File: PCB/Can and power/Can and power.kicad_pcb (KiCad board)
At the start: 2 copper layers, 37.5 x 35 mm, 34 parts, among them J1 TPS54232DR, J2 ESP32, J3 12V, J4 C_H, J5 C_L, J6 GND, U1 SN65HVD230

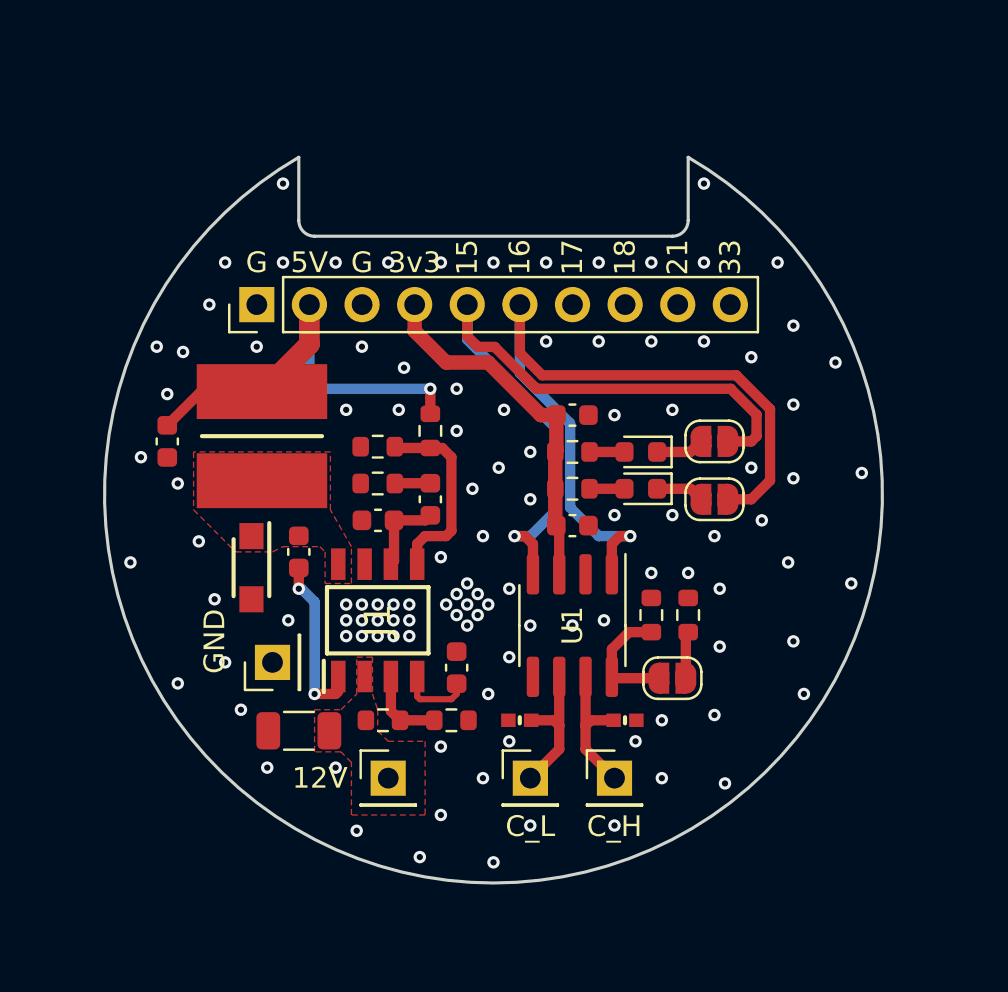
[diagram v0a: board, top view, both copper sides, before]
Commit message: Added protection diode on voltage input
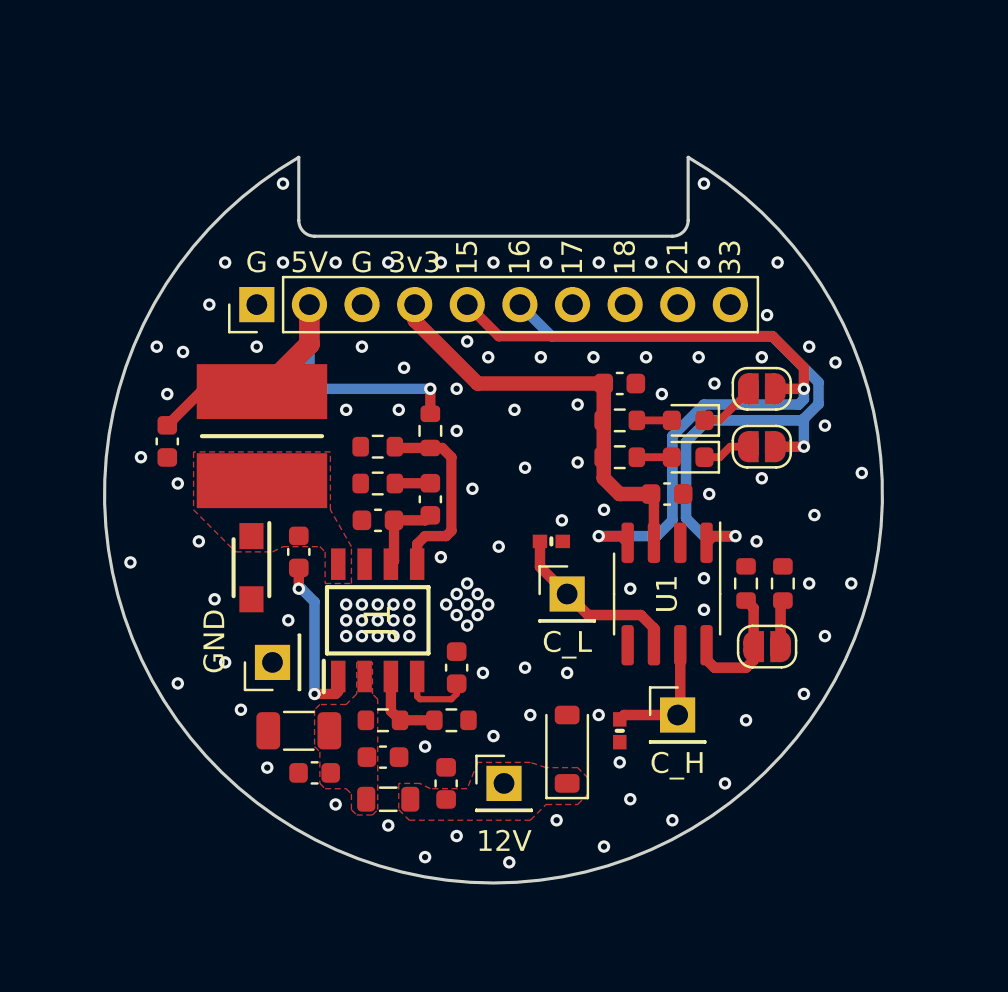
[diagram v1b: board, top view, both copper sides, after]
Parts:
- removed G***: LOGO, LOGO
- added C1: 0.1uF 50V, Capacitor_SMD:C_0603_1608Metric, F.Cu at (137.7, 114.0)
- added C2: 0.1uF 50V, Capacitor_SMD:C_0603_1608Metric, F.Cu at (134.7, 112.7)
- added C5: 1uF, Capacitor_SMD:C_0603_1608Metric, F.Cu at (131.4, 113.5)
- added D6: 18V, Diode_SMD:D_SOD-123, F.Cu at (143.6, 112.3)
- added FB1: 120R@100MHz, Inductor_SMD:L_0805_2012Metric, F.Cu at (134.9, 114.7)
- moved J5 9.07 mm to (143.6, 104.8)
- moved D2 8.77 mm to (142.8, 102.3), turned to 0 degrees
- moved J3 5.59 mm to (140.5, 114.0)
- moved C3 4.82 mm to (148.4, 100.0)
- moved JP1 4.82 mm to (153.2, 107.4)
- moved R2 4.82 mm to (154.0, 104.3)
- moved R8 4.82 mm to (152.2, 104.3)
- moved U1 4.82 mm to (148.4, 104.8)
- moved J4 4.31 mm to (148.9, 110.7)
- moved JP3 3.42 mm to (153.0, 97.7)
- moved JP2 3.42 mm to (153.0, 94.9)
- moved C4 2.75 mm to (146.1, 94.7)
- moved D4 2.75 mm to (149.4, 96.4)
- moved D5 2.75 mm to (149.4, 98.2)
- moved R1 2.75 mm to (146.1, 96.4)
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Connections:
- C9 pad 1: +12V -> Net-(J1-VIN)
- J1 pad 2: +12V -> Net-(J1-VIN)
- Ren1 pad 2: +12V -> Net-(J1-VIN)
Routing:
- net GPIO16: track 38.2 -> 34.8 mm, vias 1 -> 2
- net +3V3: track 17.6 -> 20.7 mm
- net Net-(J5-Pin_1): track 6.93 -> 8.78 mm
- net Net-(J4-Pin_1): track 6.93 -> 6.30 mm
- net GPIO15: track 36.3 -> 37.0 mm, vias 1 -> 2
- net Net-(D4-K): track 2.33 -> 2.83 mm
- added copper zone on F.Cu, net Net-(J1-VIN)

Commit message: V4 PCB
Ren1 and Ren2 values might not be discriminating enough
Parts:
- added G***: LOGO, Library:QRCode, B.Cu at (134.4, 99.5)

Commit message: Schematics and PCB update
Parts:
- D1, D2: footprint SamacSys_Parts:DIONC1005X43N -> DIY:DIONC1005X43N
- D3: footprint SamacSys_Parts:SODFL3617X108N -> DIY:SODFL3617X108N
- J1: footprint SamacSys_Parts:SOIC127P600X175-8N -> DIY:SOIC127P600X175-8N
- L2: footprint SamacSys_Parts:INDC6060X450N -> DIY:INDC6060X450N

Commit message: Universal cutout integration
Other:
- board size 37.5 x 35 mm -> 43.4 x 43.5 mm

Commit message: Pre-PCB layout
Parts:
- removed G***: LOGO, Library:QRCode
- removed J2: ESP32, Connector_PinHeader_2.54mm:PinHeader_1x10_P2.54mm_Vertical
- removed JP2, JP3: SolderJumper_2_Open, Jumper:SolderJumper-2_P1.3mm_Open_RoundedPad1.0x1.5mm
- added J7: Car connector, Connector_PinHeader_2.54mm:PinHeader_1x05_P2.54mm_Vertical, F.Cu at (137.3, 91.1)
- added JP4: Use IGN, Jumper:SolderJumper-2_P1.3mm_Bridged_RoundedPad1.0x1.5mm, B.Cu at (144.3, 98.0)
- added REF**: MountingHole_2.2mm_M2, MountingHole:MountingHole_2.2mm_M2, F.Cu at (151.5, 115.8)
- added REF**: MountingHole_2.2mm_M2, MountingHole:MountingHole_2.2mm_M2, F.Cu at (161.7, 100.0)
- added REF**: MountingHole_2.2mm_M2, MountingHole:MountingHole_2.2mm_M2, F.Cu at (129.0, 86.1)
- added REF**: MountingHole_2.2mm_M2, MountingHole:MountingHole_2.2mm_M2, F.Cu at (126.5, 86.2)
- added REF**: MountingHole_2.2mm_M2, MountingHole:MountingHole_2.2mm_M2, F.Cu at (139.9, 119.2)
- added REF**: MountingHole_2.2mm_M2, MountingHole:MountingHole_2.2mm_M2, F.Cu at (128.4, 115.8)
- added REF**: MountingHole_2.2mm_M2, MountingHole:MountingHole_2.2mm_M2, F.Cu at (128.4, 84.2)
- added REF**: MountingHole_2.2mm_M2, MountingHole:MountingHole_2.2mm_M2, F.Cu at (151.5, 84.2)
- added REF**: MountingHole_2.2mm_M2, MountingHole:MountingHole_2.2mm_M2, F.Cu at (126.5, 113.8)
- added REF**: MountingHole_2.2mm_M2, MountingHole:MountingHole_2.2mm_M2, F.Cu at (158.7, 104.9)
- J3: value 12V -> HDR_143_1; footprint Connector_PinHeader_2.54mm:PinHeader_1x01_P2.54mm_Vertical -> Connector_PinSocket_1.27mm:PinSocket_2x07_P1.27mm_Vertical; moved to B.Cu
- J4: value C_H -> HDR_143_2; footprint Connector_PinHeader_2.54mm:PinHeader_1x01_P2.54mm_Vertical -> Connector_PinSocket_1.27mm:PinSocket_2x07_P1.27mm_Vertical; moved to B.Cu
- J5: value C_L -> SKT_146; footprint Connector_PinHeader_2.54mm:PinHeader_1x01_P2.54mm_Vertical -> Connector_PinSocket_1.27mm:PinSocket_2x10_P1.27mm_Vertical; moved to B.Cu
- J6: value GND -> HDR_175; footprint Connector_PinHeader_2.54mm:PinHeader_1x01_P2.54mm_Vertical -> Connector_PinSocket_2.54mm:PinSocket_1x08_P2.54mm_Vertical
- JP1: value SolderJumper_2_Open -> High RS
- moved J4 29.2 mm to (136.2, 84.4), turned to -90 degrees
- moved JP1 28.0 mm to (128.6, 94.0)
- moved R2 28.0 mm to (129.3, 90.9)
- moved R8 28.0 mm to (127.6, 90.9)
- moved C11 25.8 mm to (146.3, 110.8), turned to 90 degrees
- moved C5 24.9 mm to (147.4, 94.4), turned to 0 degrees
- moved L2 23.7 mm to (150.7, 106.5), turned to -90 degrees
- moved D5 23.7 mm to (127.6, 107.4), turned to -90 degrees
- moved FB1 23.3 mm to (143.8, 93.1), turned to 0 degrees
- moved D3 23.1 mm to (151.2, 100.3), turned to 90 degrees
- moved C9 23.1 mm to (148.1, 96.4), turned to 0 degrees
- moved C4 22.2 mm to (131.9, 111.7)
- moved D1 21.5 mm to (134.9, 93.1), turned to 90 degrees
- moved D6 21.4 mm to (142.7, 91.0), turned to 0 degrees
- moved C1 20.3 mm to (141.0, 93.9), turned to 90 degrees
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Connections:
- D1 pad 1: Net-(J4-Pin_1) -> /CAN_H
- D2 pad 1: Net-(J5-Pin_1) -> /CAN_L
- D4 pad 1: Net-(D4-K) -> RX_CAN
- D5 pad 1: Net-(D5-K) -> TX_CAN
- J3 pad 1: +12V -> /143_GPIO0
- J4 pad 1: Net-(J4-Pin_1) -> /143_GPIO45
- J5 pad 1: Net-(J5-Pin_1) -> /146_GPIO13
- J6 pad 1: GND -> /175_GPIO18
- Ren1 pad 1: Net-(J1-EN) -> Net-(JP4-A)
- Ren2 pad 2: Net-(J1-EN) -> Net-(JP4-A)
- U1 pad 1: GPIO16 -> TX_CAN
- U1 pad 4: GPIO15 -> RX_CAN
- U1 pad 6: Net-(J5-Pin_1) -> /CAN_L
- U1 pad 7: Net-(J4-Pin_1) -> /CAN_H
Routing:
- net GPIO15: track 37.0 -> 0.00 mm, vias 2 -> 0
- net GPIO16: track 34.8 -> 0.00 mm, vias 2 -> 0
- net +3V3: track 20.7 -> 7.46 mm
- net VSYS: track 21.4 -> 8.90 mm, vias 1 -> 0
- net /CAN_H: track 0.00 -> 11.6 mm
- net /CAN_L: track 0.00 -> 10.6 mm
- net Net-(J5-Pin_1): track 8.78 -> 0.00 mm
- net Net-(J1-BOOT): track 8.39 -> 1.91 mm, vias 2 -> 1
- net Net-(J4-Pin_1): track 6.30 -> 0.00 mm
- net Net-(JP4-A): track 0.00 -> 4.96 mm, vias 0 -> 1
- net Net-(D4-K): track 2.83 -> 0.00 mm
- net TX_CAN: track 0.00 -> 2.46 mm
- net RX_CAN: track 0.00 -> 2.46 mm
- net Net-(D5-K): track 2.33 -> 0.00 mm
- net Net-(JP1-B): track 6.31 -> 7.95 mm
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- removed copper zone on B.Cu, net GND
- removed copper zone on F.Cu, net GND
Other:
- copper layers 2 -> 4
- board text removed: "15"
- board text removed: "16"
- board text removed: "17"
- board text removed: "18"
- board text removed: "21"
- board text removed: "33"
- board text removed: "3v3"
- board text removed: "5V"
- board text removed: "G"
- board text removed: "MRR"
- board text removed: "WAYWAYWAY"
- board text removed: "rev ${REVISION}"

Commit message: Need ERC corrections
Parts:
- J7: footprint Connector_PinHeader_2.54mm:PinHeader_1x05_P2.54mm_Vertical -> Connector_PinHeader_2.54mm:PinHeader_1x04_P2.54mm_Vertical
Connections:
- J3 pad 4: /143_GPIO2 -> RX_CAN
- J3 pad 6: /143_GPIO3 -> TX_CAN
- J5 pad 1: /146_GPIO13 -> TX_CAN
- J5 pad 3: /146_GPIO12 -> RX_CAN
- J6 pad 4: /175_RXD -> RX_CAN
- J6 pad 5: /175_TXD -> TX_CAN
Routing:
- net +3V3: track 7.46 -> 76.7 mm, vias 0 -> 1
- net TX_CAN: track 2.46 -> 62.2 mm, vias 0 -> 3
- net VSYS: track 8.90 -> 68.6 mm, vias 0 -> 13
- net RX_CAN: track 2.46 -> 60.6 mm, vias 0 -> 2
- added copper zone on B.Cu, net GND
- added copper zone on F.Cu, net GND
- added copper zone on In1.Cu, net GND
- added copper zone on In2.Cu, net GND
- added copper zone on B.Cu, net VSYS
- added copper zone on F.Cu, net VSYS

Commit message: Projectification, correct footprints
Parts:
- removed REF** (x10): MountingHole_2.2mm_M2, MountingHole:MountingHole_2.2mm_M2
- added F1: 30V 500mA 2.5A-100ms, Fuse:Fuse_1210_3225Metric, F.Cu at (136.4, 95.2)
- added RV1: B72520T0140K062, Fuse:Fuse_1206_3216Metric, F.Cu at (138.6, 90.0)
- D1, D2: footprint DIY:DIONC1005X43N -> Project_footprints:DIONC1005X43N
- D3: footprint DIY:SODFL3617X108N -> Project_footprints:SODFL3617X108N
- J1: footprint DIY:SOIC127P600X175-8N -> Project_footprints:SOIC127P600X175-8N
- J3, J4: footprint Connector_PinSocket_1.27mm:PinSocket_2x07_P1.27mm_Vertical -> Connector_PinHeader_1.27mm:PinHeader_2x07_P1.27mm_Vertical
- J6: footprint Connector_PinSocket_2.54mm:PinSocket_1x08_P2.54mm_Vertical -> Connector_PinHeader_2.54mm:PinHeader_1x08_P2.54mm_Vertical; moved to B.Cu
- J7: footprint Connector_PinHeader_2.54mm:PinHeader_1x04_P2.54mm_Vertical -> Connector_JST:JST_EH_B4B-EH-A_1x04_P2.50mm_Vertical
- L2: footprint DIY:INDC6060X450N -> Project_footprints:INDC6060X450N
- moved J7 10.1 mm to (137.3, 101.3), turned to -90 degrees
- moved D1 8.21 mm to (133.8, 101.2)
- moved D2 7.08 mm to (133.8, 103.7)
- moved J3 1.26 mm to (136.2, 115.6)
- moved J4 1.26 mm to (136.2, 83.1)
- turned J6 to 180 degrees
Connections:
- C1 pad 2: +12V -> Net-(D6-K)
- D6 pad 1: +12V -> Net-(D6-K)
- FB1 pad 1: +12V -> Net-(D6-K)
- J3 pad 1: /143_GPIO0 -> /143_GPIO1
- J3 pad 10: /143_GPIO6 -> GND
- J3 pad 11: VSYS -> /143_USB_N
- J3 pad 12: /143_USB_N -> VSYS
- J3 pad 13: /143_VBAT -> /143_USB_P
- J3 pad 14: /143_USB_P -> /143_VBAT
- J3 pad 2: /143_GPIO1 -> /143_GPIO0
- J3 pad 3: /143_GPIO7 -> RX_CAN
- J3 pad 4: RX_CAN -> /143_GPIO7
- J3 pad 5: /143_GPIO17 -> TX_CAN
- J3 pad 6: TX_CAN -> /143_GPIO17
- J3 pad 7: /143_GPIO16 -> /143_GPIO5
- J3 pad 8: /143_GPIO5 -> /143_GPIO16
- J3 pad 9: GND -> /143_GPIO6
- J4 pad 1: /143_GPIO45 -> +3V3
- J4 pad 10: /143_SDA -> /143_GPIO39
- J4 pad 11: /143_GPIO38 -> /143_SCL
- J4 pad 12: /143_SCL -> /143_GPIO38
- J4 pad 13: /143_GPIO18 -> +3V3
- J4 pad 14: +3V3 -> /143_GPIO18
- J4 pad 2: +3V3 -> /143_GPIO45
- J4 pad 3: /143_GPIO46 -> /143_TXD
- J4 pad 4: /143_TXD -> /143_GPIO46
- J4 pad 5: /143_GPIO41 -> /143_RXD
- J4 pad 6: /143_RXD -> /143_GPIO41
- J4 pad 7: /143_GPIO40 -> GND
- J4 pad 8: GND -> /143_GPIO40
- J4 pad 9: /143_GPIO39 -> /143_SDA
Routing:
- net Net-(J1-BOOT): track 1.91 -> 4.77 mm, vias 1 -> 0
- net /CAN_H: track 11.6 -> 14.0 mm
- net /CAN_L: track 10.6 -> 11.7 mm
- net RX_CAN: track 60.6 -> 59.6 mm
- net VSYS: track 68.6 -> 69.2 mm
- added copper zone on F.Cu, net Net-(D6-K)

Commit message: UniverCan v6.0
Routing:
- net GND: vias 15 -> 198
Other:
- board text added: "(c) ${COMPANY} - ${ISSUE_DATE} ${TITLE} v${REVISION}"
- board text added: "1.43in"
- board text added: "1.46in"
- board text added: "1.75in"
- board text added: "12V"
- board text added: "3V3"
- board text added: "CAN_H"
- board text added: "CAN_L"
- board text added: "GND"
- board text added: "RX"
- board text added: "TX"
- board text added: "VSYS"
- board text added: "~{RX}"
- board text added: "~{TX}"
- board text added: "~{Use IGN}"
